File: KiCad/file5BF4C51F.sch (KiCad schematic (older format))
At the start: 6 parts, among them J401 CONN_01X06, J402 CONN_01X10, J403 CONN_01X10

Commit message: Changes for FlexFox80
Wholesale changes for new project.
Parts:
- J401: symbol ARDF-2-Band-MiniTx-rescue:CONN_01X06 -> FlexFox80-rescue:CONN_01X06-ARDF-2-Band-MiniTx-rescue
- J402, J403: symbol ARDF-2-Band-MiniTx-rescue:CONN_01X10 -> FlexFox80-rescue:CONN_01X10-ARDF-2-Band-MiniTx-rescue
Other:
- note added: "BOM-ONLY: Flex Fox 80 ARDF Transmitter"
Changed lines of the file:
@@
 $EndComp
 $Comp
-L ARDF-2-Band-MiniTx-rescue:CONN_01X06 J401
+L FlexFox80-rescue:CONN_01X06-ARDF-2-Band-MiniTx-rescue J401
 U 1 1 5C10B0E5
 P 3100 3700
@@
 $EndComp
 $Comp
-L ARDF-2-Band-MiniTx-rescue:CONN_01X10 J402
+L FlexFox80-rescue:CONN_01X10-ARDF-2-Band-MiniTx-rescue J402
 U 1 1 5C10B110
 P 3750 3850
@@
 $EndComp
 $Comp
-L ARDF-2-Band-MiniTx-rescue:CONN_01X10 J403
+L FlexFox80-rescue:CONN_01X10-ARDF-2-Band-MiniTx-rescue J403
 U 1 1 5C10B14B
 P 4250 3850
@@
 Text Notes 2900 3250 0    61   ~ 12
 Header sockets for Huzzah board
+Text Notes 7200 6750 0    118  ~ 24
+BOM-ONLY: Flex Fox 80 ARDF Transmitter
 $EndSCHEMATC

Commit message: Updates to Schematic
Updates to Schematic
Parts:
- added PH?: Power Pole Staple, symbol Device:PinlessHardware
- added PH? (x2): Power Pole Pin, symbol Device:PinlessHardware
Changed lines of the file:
@@
 Text Notes 7200 6750 0    118  ~ 24
 BOM-ONLY: Flex Fox 80 ARDF Transmitter
+$Comp
+L Device:PinlessHardware PH?
+U 1 1 607EA3F6
+P 5700 3000
+F 0 "PH?" H 5878 3179 61  0000 L CNB
+F 1 "Power Pole Staple" H 5878 3071 61  0000 L CNB
+F 2 "" H 5700 3000 39  0001 C CNN
+F 3 "" H 5700 3000 39  0001 C CNN
+F 4 "2243-114555P2-ND" H 5700 3000 50  0001 C CNN "Part No."
+F 5 "<a href=\"https://www.digikey.com/products/en?keywords=2243-114555P2-ND\">Link</a>" H 5700 3000 50  0001 C CNN "Link"
+F 6 "TH" H 5700 3000 50  0001 C CNN "Manufacturer"
+F 7 "TH" H 5700 3000 50  0001 C CNN "Manufacturer PN"
+F 8 "TH" H 5700 3000 50  0001 C CNN "Description"
+	1    5700 3000
+	1    0    0    -1
+$EndComp
+$Comp
+L Device:PinlessHardware PH?
+U 1 1 607EC98E
+P 5550 3600
+F 0 "PH?" H 5728 3779 61  0000 L CNB
+F 1 "Power Pole Pin" H 5728 3671 61  0000 L CNB
+F 2 "" H 5550 3600 39  0001 C CNN
+F 3 "" H 5550 3600 39  0001 C CNN
+F 4 "2243-1377G2-BK-ND" H 5550 3600 50  0001 C CNN "Part No."
+F 5 "<a href=\"https://www.digikey.com/products/en?keywords=2243-1377G2-BK-ND\">Link</a>" H 5550 3600 50  0001 C CNN "Link"
+F 6 "TH" H 5550 3600 50  0001 C CNN "Manufacturer"
+F 7 "TH" H 5550 3600 50  0001 C CNN "Manufacturer PN"
+F 8 "TH" H 5550 3600 50  0001 C CNN "Description"
+	1    5550 3600
+	1    0    0    -1
+$EndComp
+$Comp
+L Device:PinlessHardware PH?
+U 1 1 607ED223
+P 5550 3850
+F 0 "PH?" H 5728 4029 61  0000 L CNB
+F 1 "Power Pole Pin" H 5728 3921 61  0000 L CNB
+F 2 "" H 5550 3850 39  0001 C CNN
+F 3 "" H 5550 3850 39  0001 C CNN
+F 4 "2243-1377G2-BK-ND" H 5550 3850 50  0001 C CNN "Part No."
+F 5 "<a href=\"https://www.digikey.com/products/en?keywords=2243-1377G2-BK-ND\">Link</a>" H 5550 3850 50  0001 C CNN "Link"
+F 6 "TH" H 5550 3850 50  0001 C CNN "Manufacturer"
+F 7 "TH" H 5550 3850 50  0001 C CNN "Manufacturer PN"
+F 8 "TH" H 5550 3850 50  0001 C CNN "Description"
+	1    5550 3850
+	1    0    0    -1
+$EndComp
 $EndSCHEMATC

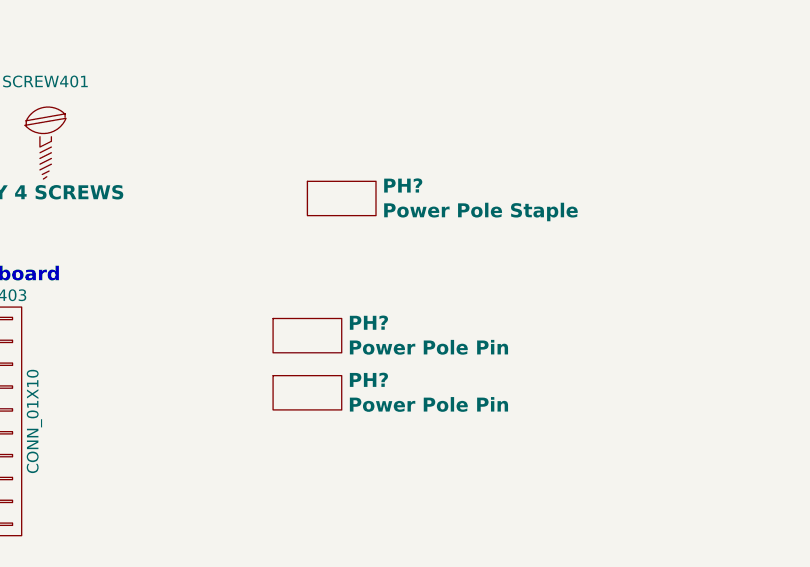
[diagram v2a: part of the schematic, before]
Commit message: Design Updates
Specifying components
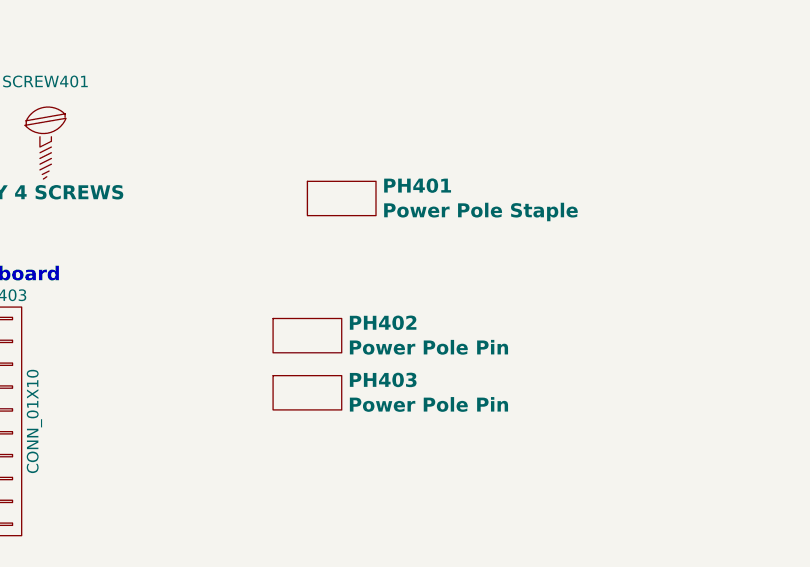
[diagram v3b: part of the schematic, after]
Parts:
- gave numbers to parts that had none: 3
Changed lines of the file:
@@
 BOM-ONLY: Flex Fox 80 ARDF Transmitter
 $Comp
-L Device:PinlessHardware PH?
+L Device:PinlessHardware PH401
 U 1 1 607EA3F6
 P 5700 3000
-F 0 "PH?" H 5878 3179 61  0000 L CNB
+F 0 "PH401" H 5878 3179 61  0000 L CNB
 F 1 "Power Pole Staple" H 5878 3071 61  0000 L CNB
 F 2 "" H 5700 3000 39  0001 C CNN
@@
 $EndComp
 $Comp
-L Device:PinlessHardware PH?
+L Device:PinlessHardware PH402
 U 1 1 607EC98E
 P 5550 3600
-F 0 "PH?" H 5728 3779 61  0000 L CNB
+F 0 "PH402" H 5728 3779 61  0000 L CNB
 F 1 "Power Pole Pin" H 5728 3671 61  0000 L CNB
 F 2 "" H 5550 3600 39  0001 C CNN
@@
 $EndComp
 $Comp
-L Device:PinlessHardware PH?
+L Device:PinlessHardware PH403
 U 1 1 607ED223
 P 5550 3850
-F 0 "PH?" H 5728 4029 61  0000 L CNB
+F 0 "PH403" H 5728 4029 61  0000 L CNB
 F 1 "Power Pole Pin" H 5728 3921 61  0000 L CNB
 F 2 "" H 5550 3850 39  0001 C CNN

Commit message: Design Updates
Updated schematics parts descriptions
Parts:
- removed J403: CONN_01X10, Oddities:Dummy_Empty, symbol FlexFox80-rescue:CONN_01X10-ARDF-2-Band-MiniTx-rescue
- removed PH402, PH403: Power Pole Pin, symbol Device:PinlessHardware
- added J403: CONN_01X10, Oddities:Dummy_Empty, symbol Connector_Generic:Conn_01x10
- J401: symbol FlexFox80-rescue:CONN_01X06-ARDF-2-Band-MiniTx-rescue -> Connector_Generic:Conn_01x06; Description (none) -> CONN HDR 6POS 0.1 GOLD SMD; Digi-Key Part No. (none) -> S5637-ND; Manufacturer (none) -> Sullins Connector Solutions; Manufacturer PN (none) -> NPPC061KFXC-RC; Part No. S5637-ND -> (none)
- J402: symbol FlexFox80-rescue:CONN_01X10-ARDF-2-Band-MiniTx-rescue -> Connector_Generic:Conn_01x10; Description (none) -> CONN HDR 10POS 0.1 GOLD SMD; Digi-Key Part No. (none) -> S5641-ND; Manufacturer (none) -> Sullins Connector Solutions; Manufacturer PN (none) -> NPPC101KFXC-RC; Part No. S5641-ND -> (none)
- PH401: footprint (none) -> Oddities:Dummy_Empty
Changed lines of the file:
@@
 $EndComp
 $Comp
-L FlexFox80-rescue:CONN_01X06-ARDF-2-Band-MiniTx-rescue J401
+L Connector_Generic:Conn_01x06 J401
 U 1 1 5C10B0E5
-P 3100 3700
-F 0 "J401" H 3100 4050 50  0000 C CNN
-F 1 "CONN_01X06" V 3200 3700 50  0000 C CNN
-F 2 "Oddities:Dummy_Empty" H 3100 3700 50  0001 C CNN
-F 3 "" H 3100 3700 50  0001 C CNN
-F 4 "S5637-ND" H 3100 3700 60  0001 C CNN "Part No."
-F 5 "<a href=\"https://www.digikey.com/product-detail/en/sullins-connector-solutions/NPPC061KFXC-RC/S5637-ND/776096\">Link</a>" H 3100 3700 60  0001 C CNN "Link"
-	1    3100 3700
+P 3100 3650
+F 0 "J401" H 3100 4000 50  0000 C CNN
+F 1 "CONN_01X06" V 3200 3650 50  0000 C CNN
+F 2 "Oddities:Dummy_Empty" H 3100 3650 50  0001 C CNN
+F 3 "" H 3100 3650 50  0001 C CNN
+F 4 "S5637-ND" H 3100 3650 50  0001 C CNN "Digi-Key Part No."
+F 5 "<a href=\"https://www.digikey.com/product-detail/en/sullins-connector-solutions/NPPC061KFXC-RC/S5637-ND/776096\">Link</a>" H 3100 3650 60  0001 C CNN "Link"
+F 6 "Sullins Connector Solutions" H 3100 3650 50  0001 C CNN "Manufacturer"
+F 7 "NPPC061KFXC-RC" H 3100 3650 50  0001 C CNN "Manufacturer PN"
+F 8 "CONN HDR 6POS 0.1 GOLD SMD" H 3100 3650 50  0001 C CNN "Description"
+	1    3100 3650
 	1    0    0    -1
 $EndComp
 $Comp
-L FlexFox80-rescue:CONN_01X10-ARDF-2-Band-MiniTx-rescue J402
+L Connector_Generic:Conn_01x10 J402
 U 1 1 5C10B110
-P 3750 3850
-F 0 "J402" H 3750 4400 50  0000 C CNN
-F 1 "CONN_01X10" V 3850 3850 50  0000 C CNN
-F 2 "Oddities:Dummy_Empty" H 3750 3850 50  0001 C CNN
-F 3 "" H 3750 3850 50  0001 C CNN
-F 4 "S5641-ND" H 3750 3850 60  0001 C CNN "Part No."
-F 5 "<a href=\"https://www.digikey.com/product-detail/en/sullins-connector-solutions/NPPC101KFXC-RC/S5641-ND/776100\">Link</a>" H 3750 3850 60  0001 C CNN "Link"
-	1    3750 3850
-	1    0    0    -1
-$EndComp
-$Comp
-L FlexFox80-rescue:CONN_01X10-ARDF-2-Band-MiniTx-rescue J403
-U 1 1 5C10B14B
-P 4250 3850
-F 0 "J403" H 4250 4400 50  0000 C CNN
-F 1 "CONN_01X10" V 4350 3850 50  0000 C CNN
-F 2 "Oddities:Dummy_Empty" H 4250 3850 50  0001 C CNN
-F 3 "" H 4250 3850 50  0001 C CNN
-F 4 "S5641-ND" H 4250 3850 60  0001 C CNN "Part No."
-F 5 "<a href=\"https://www.digikey.com/product-detail/en/sullins-connector-solutions/NPPC101KFXC-RC/S5641-ND/776100\">Link</a>" H 4250 3850 60  0001 C CNN "Link"
-	1    4250 3850
+P 3750 3800
+F 0 "J402" H 3750 4350 50  0000 C CNN
+F 1 "CONN_01X10" V 3850 3800 50  0000 C CNN
+F 2 "Oddities:Dummy_Empty" H 3750 3800 50  0001 C CNN
+F 3 "" H 3750 3800 50  0001 C CNN
+F 4 "S5641-ND" H 3750 3800 50  0001 C CNN "Digi-Key Part No."
+F 5 "<a href=\"https://www.digikey.com/product-detail/en/sullins-connector-solutions/NPPC101KFXC-RC/S5641-ND/776100\">Link</a>" H 3750 3800 60  0001 C CNN "Link"
+F 6 "Sullins Connector Solutions" H 3750 3800 50  0001 C CNN "Manufacturer"
+F 7 "NPPC101KFXC-RC" H 3750 3800 50  0001 C CNN "Manufacturer PN"
+F 8 "CONN HDR 10POS 0.1 GOLD SMD" H 3750 3800 50  0001 C CNN "Description"
+	1    3750 3800
 	1    0    0    -1
 $EndComp
@@
 NoConn ~ 2900 3850
 NoConn ~ 2900 3950
-Text Notes 2900 3250 0    61   ~ 12
+Text Notes 2900 3150 0    61   ~ 12
 Header sockets for Huzzah board
 Text Notes 7200 6750 0    118  ~ 24
@@
 F 0 "PH401" H 5878 3179 61  0000 L CNB
 F 1 "Power Pole Staple" H 5878 3071 61  0000 L CNB
-F 2 "" H 5700 3000 39  0001 C CNN
+F 2 "Oddities:Dummy_Empty" H 5700 3000 39  0001 C CNN
 F 3 "" H 5700 3000 39  0001 C CNN
 F 4 "2243-114555P2-ND" H 5700 3000 50  0001 C CNN "Part No."
@@
 $EndComp
 $Comp
-L Device:PinlessHardware PH402
-U 1 1 607EC98E
-P 5550 3600
-F 0 "PH402" H 5728 3779 61  0000 L CNB
-F 1 "Power Pole Pin" H 5728 3671 61  0000 L CNB
-F 2 "" H 5550 3600 39  0001 C CNN
-F 3 "" H 5550 3600 39  0001 C CNN
-F 4 "2243-1377G2-BK-ND" H 5550 3600 50  0001 C CNN "Part No."
-F 5 "<a href=\"https://www.digikey.com/products/en?keywords=2243-1377G2-BK-ND\">Link</a>" H 5550 3600 50  0001 C CNN "Link"
-F 6 "TH" H 5550 3600 50  0001 C CNN "Manufacturer"
-F 7 "TH" H 5550 3600 50  0001 C CNN "Manufacturer PN"
-F 8 "TH" H 5550 3600 50  0001 C CNN "Description"
-	1    5550 3600
+L Connector_Generic:Conn_01x10 J403
+U 1 1 60AEF502
+P 4250 3800
+F 0 "J403" H 4250 4350 50  0000 C CNN
+F 1 "CONN_01X10" V 4350 3800 50  0000 C CNN
+F 2 "Oddities:Dummy_Empty" H 4250 3800 50  0001 C CNN
+F 3 "" H 4250 3800 50  0001 C CNN
+F 4 "S5641-ND" H 4250 3800 50  0001 C CNN "Digi-Key Part No."
+F 5 "<a href=\"https://www.digikey.com/product-detail/en/sullins-connector-solutions/NPPC101KFXC-RC/S5641-ND/776100\">Link</a>" H 4250 3800 60  0001 C CNN "Link"
+F 6 "Sullins Connector Solutions" H 4250 3800 50  0001 C CNN "Manufacturer"
+F 7 "NPPC101KFXC-RC" H 4250 3800 50  0001 C CNN "Manufacturer PN"
+F 8 "CONN HDR 10POS 0.1 GOLD SMD" H 4250 3800 50  0001 C CNN "Description"
+	1    4250 3800
 	1    0    0    -1
 $EndComp
-$Comp
-L Device:PinlessHardware PH403
-U 1 1 607ED223
-P 5550 3850
-F 0 "PH403" H 5728 4029 61  0000 L CNB
-F 1 "Power Pole Pin" H 5728 3921 61  0000 L CNB
-F 2 "" H 5550 3850 39  0001 C CNN
-F 3 "" H 5550 3850 39  0001 C CNN
-F 4 "2243-1377G2-BK-ND" H 5550 3850 50  0001 C CNN "Part No."
-F 5 "<a href=\"https://www.digikey.com/products/en?keywords=2243-1377G2-BK-ND\">Link</a>" H 5550 3850 50  0001 C CNN "Link"
-F 6 "TH" H 5550 3850 50  0001 C CNN "Manufacturer"
-F 7 "TH" H 5550 3850 50  0001 C CNN "Manufacturer PN"
-F 8 "TH" H 5550 3850 50  0001 C CNN "Description"
-	1    5550 3850
-	1    0    0    -1
-$EndComp
